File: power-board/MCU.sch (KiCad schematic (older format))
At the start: 29 parts, among them CON1 AVR-ISP-6, IC1 ATMEGA328P-A, SW1 BOOT, SW2 RESET, Y1 20MHz

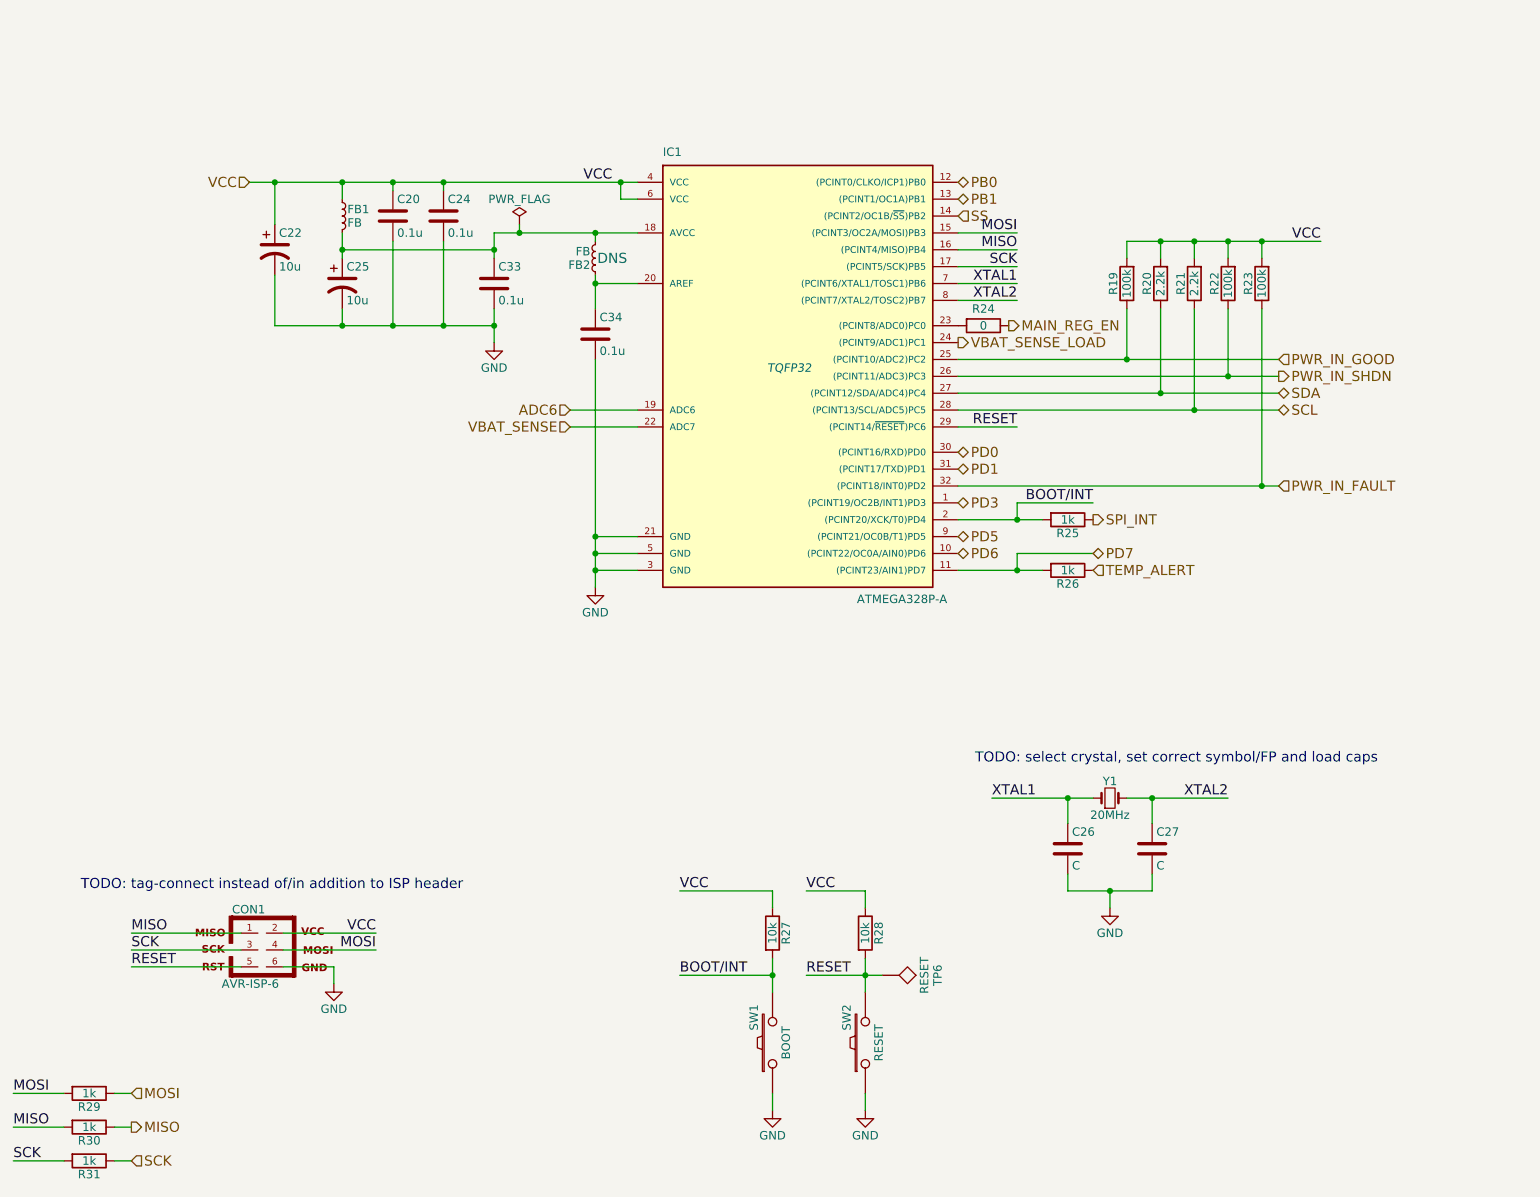
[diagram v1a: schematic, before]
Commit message: switched to XMEGA A4U
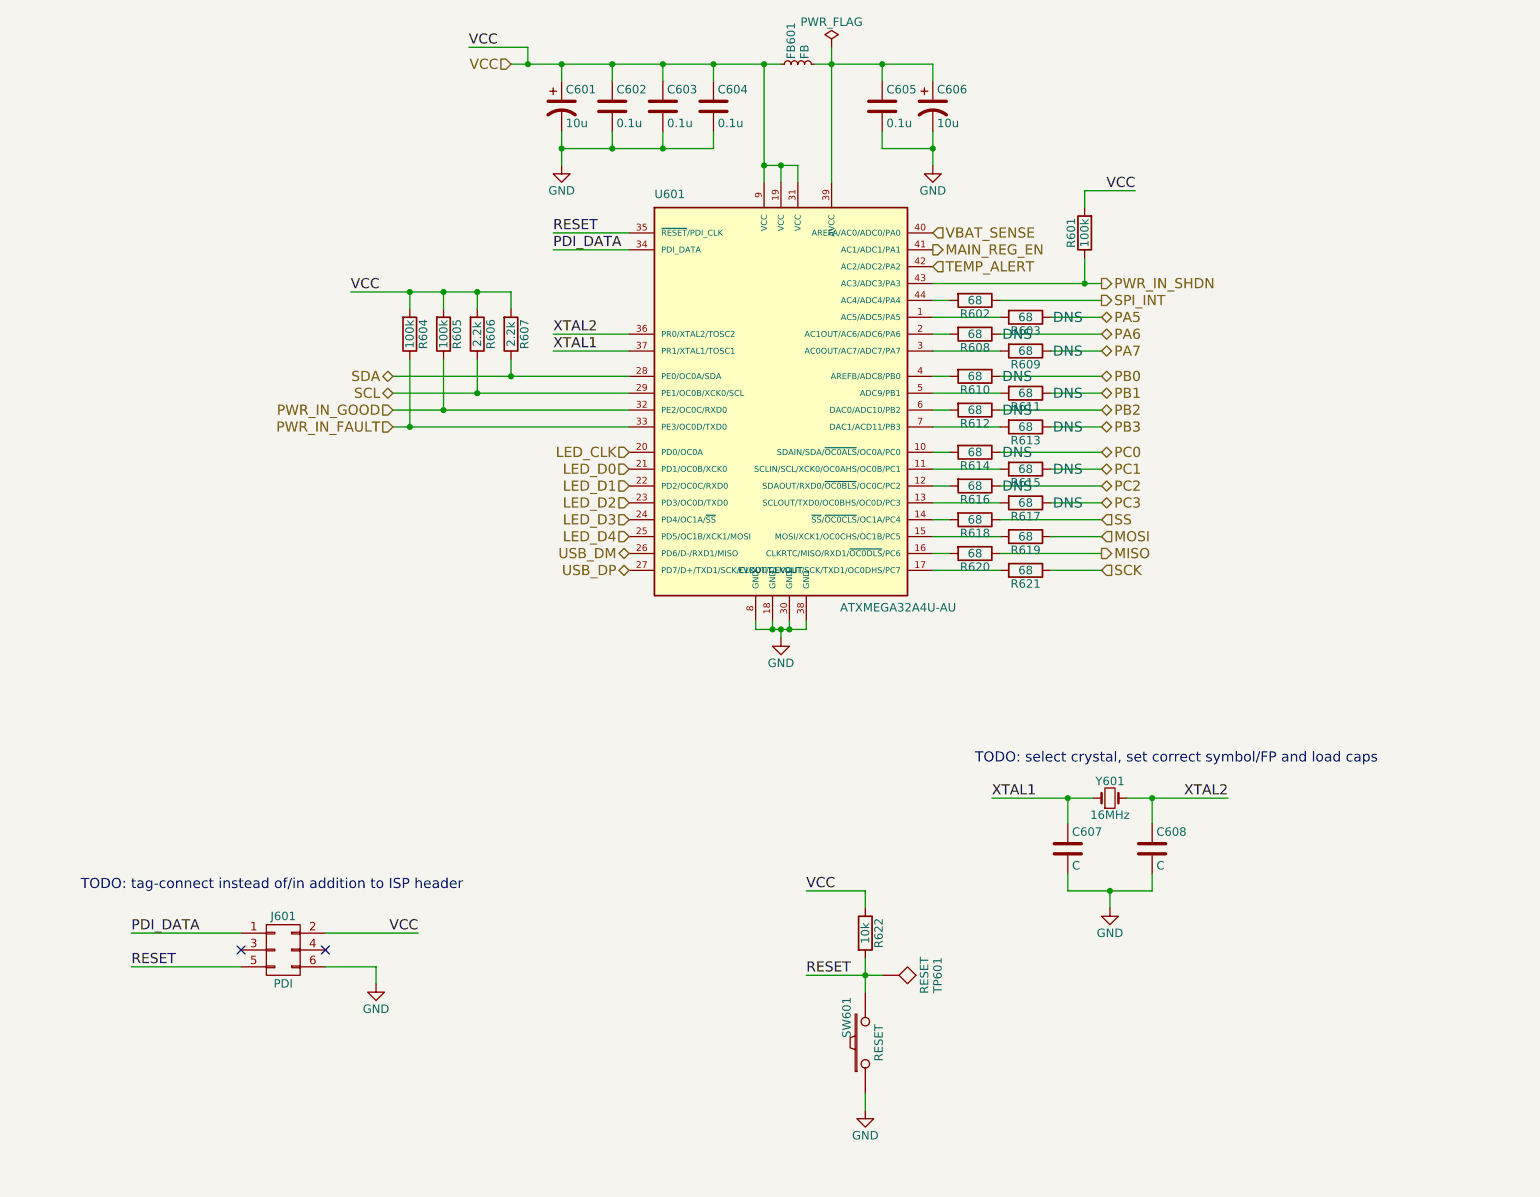
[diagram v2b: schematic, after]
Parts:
- removed C24, C33, C34: 0.1u, symbol C
- removed CON1: AVR-ISP-6, AVR-ISP-6, symbol AVR-ISP-6
- removed FB2: FB, symbol L_Small
- removed IC1: ATMEGA328P-A, TQFP32, symbol ATMEGA328P-A
- removed R24: 0, symbol R
- removed R25, R26, R29, R30, R31: 1k, symbol R
- removed R27: 10k, symbol R
- removed SW1: BOOT, symbol SW_PUSH
- added C603, C604, C605: 0.1u, symbol C
- added J601: PDI, symbol CONN_02X03
- added R602, R603, R608, R609, R610, R611, R612, R613, R614, R615, R616, R617, R618, R619, R620, R621: 68, symbol R
- added U601: ATXMEGA32A4U-AU, TQFP44, symbol ATXMEGA32A4U-AU
- Y601: renamed from Y1; value 20MHz -> 16MHz
- renumbered C22 to C601, C20 to C602, C25 to C606, C26 to C607, C27 to C608, FB1 to FB601, R23 to R601, R22 to R604, R19 to R605, R21 to R606, R20 to R607, R28 to R622, SW2 to SW601, TP6 to TP601
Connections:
- net GND: now also C603.2, C604.2, C605.2, J601.6 (P6), U601.18 (GND), U601.30 (GND), U601.38 (GND), U601.8 (GND)
- net MAIN_REG_EN: now also U601.41 (AC1/ADC1/PA1)
- net MISO: now also R620.1
- net MOSI: now also R619.1
- net PB0: now also R610.1
- net PB1: now also R611.1
- net PWR_IN_FAULT: now also R604.1, U601.33 (PE3/OC0D/TXD0); no longer R601.1
- net PWR_IN_GOOD: now also U601.32 (PE2/OC0C/RXD0)
- net PWR_IN_SHDN: now also R601.1, U601.43 (AC3/ADC3/PA3); no longer R604.1
- net RESET: now also J601.5 (P5), U601.35 (~RESET~/PDI_CLK)
- net SCK: now also R621.1
- net SCL: now also U601.29 (PE1/OC0B/XCK0/SCL)
- net SDA: now also U601.28 (PE0/OC0A/SDA)
- net SPI_INT: now also R602.1
- net SS: now also R618.1
- net TEMP_ALERT: now also U601.42 (AC2/ADC2/PA2)
- net VBAT_SENSE: now also U601.40 (AREFA/AC0/ADC0/PA0)
- net VCC: now also C603.1, C604.1, J601.2 (P2), U601.19 (VCC), U601.31 (VCC), U601.9 (VCC)
- net XTAL1: now also U601.37 (PR1/XTAL1/TOSC1)
- net XTAL2: now also U601.36 (PR0/XTAL2/TOSC2)
- net at C606.1, FB601.2: now also C605.1, U601.39 (AVCC)
- new net: R603.2, U601.1 (AC5/ADC5/PA5)
- new net: R614.2, U601.10 (SDAIN/SDA/~OC0ALS~/OC0A/PC0)
- new net: R615.2, U601.11 (SCLIN/SCL/XCK0/OC0AHS/OC0B/PC1)
- new net: R616.2, U601.12 (SDAOUT/RXD0/~OC0BLS~/OC0C/PC2)
- new net: R617.2, U601.13 (SCLOUT/TXD0/OC0BHS/OC0D/PC3)
- new net: R618.2, U601.14 (~SS~/~OC0CLS~/OC1A/PC4)
- new net: R619.2, U601.15 (MOSI/XCK1/OC0CHS/OC1B/PC5)
- new net: R620.2, U601.16 (CLKRTC/MISO/RXD1/~OC0DLS~/PC6)
- new net: R621.2, U601.17 (EVOUT/CLKOUT/SCK/TXD1/OC0DHS/PC7)
- new net: R608.2, U601.2 (AC1OUT/AC6/ADC6/PA6)
- new net: R609.2, U601.3 (AC0OUT/AC7/ADC7/PA7)
- new net: R610.2, U601.4 (AREFB/ADC8/PB0)
- new net: R602.2, U601.44 (AC4/ADC4/PA4)
- new net: R611.2, U601.5 (ADC9/PB1)
- new net: R612.2, U601.6 (DAC0/ADC10/PB2)
- new net: R613.2, U601.7 (DAC1/ACD11/PB3)
- new net LED_CLK: U601.20 (PD0/OC0A)
- new net LED_D0: U601.21 (PD1/OC0B/XCK0)
- new net LED_D1: U601.22 (PD2/OC0C/RXD0)
- new net LED_D2: U601.23 (PD3/OC0D/TXD0)
- new net LED_D3: U601.24 (PD4/OC1A/~SS~)
- new net LED_D4: U601.25 (PD5/OC1B/XCK1/MOSI)
- new net PA5: R603.1
- new net PA6: R608.1
- new net PA7: R609.1
- new net PB2: R612.1
- new net PB3: R613.1
- new net PC0: R614.1
- new net PC1: R615.1
- new net PC2: R616.1
- new net PC3: R617.1
- new net PDI_DATA: J601.1 (P1), U601.34 (PDI_DATA)
- new net USB_DM: U601.26 (PD6/D-/RXD1/MISO)
- new net USB_DP: U601.27 (PD7/D+/TXD1/SCK/CLKOUT/EVOUT)
- no-connect marks 0 -> 2
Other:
- moved on the sheet: C601, C602, C606, FB601, R601, R604, R605, R606, R607

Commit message: routed board
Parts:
- C601, C606: footprint (none) -> Capacitors_SMD:C_0805
- C602, C603, C604, C605: footprint (none) -> Capacitors_SMD:C_0603
- C607, C608: value C -> 26p; footprint (none) -> Capacitors_SMD:C_0805; MFG (none) -> Johanson Dielectrics Inc.; MPN (none) -> 500R15N270KV4T
- FB601: footprint (none) -> Resistors_SMD:R_0805; MFG (none) -> TDK; MPN (none) -> MPZ2012S102AT000
- J601: footprint (none) -> Connectors:Tag-Connect_TC2030-IDC-NL
- R601: value 100k -> 68; footprint (none) -> Resistors_SMD:R_0603; MFG Vishay / Draloric -> Yageo; MPN RCA0603100KJNEC -> RC0603JR-0768RL; Note (none) -> DNS
- R602, R603, R608, R609, R610, R611, R612, R613, R614, R615, R618, R619, R620, R621: footprint (none) -> Resistors_SMD:R_0603; MFG (none) -> Yageo; MPN (none) -> RC0603JR-0768RL
- R604, R605: footprint (none) -> Resistors_SMD:R_0603; MFG Vishay / Draloric -> Yageo; MPN RCA0603100KJNEC -> RC0603JR-07100KL
- R606, R607: footprint (none) -> Resistors_SMD:R_0603; MFG (none) -> Yageo; MPN (none) -> RC0603JR-072K2L
- R616, R617: footprint (none) -> Resistors_SMD:R_0603; MFG (none) -> Yageo; MPN (none) -> RC0603JR-0768RL; Note DNS -> (none)
- R622: footprint (none) -> Resistors_SMD:R_0603
- SW601: footprint (none) -> Buttons_Switches_SMD:SW_SPST_EVPBF; MFG TE Connectivity -> Panasonic Electronic Components; MPN FSM2JSMAATR -> EVP-BFAC1A000
- TP601: footprint (none) -> Connectors:PINTST
- U601: footprint TQFP44 -> Housings_QFP:TQFP-44_10x10mm_Pitch0.8mm; MFG (none) -> Microchip Technology; MPN (none) -> ATXMEGA32A4U-AU
- Y601: footprint (none) -> Crystals:Crystal_SMD_Abracon_ABM3-2pin_5.0x3.2mm_HandSoldering; MFG (none) -> Abracon; MPN (none) -> ABM3-16.000MHZ-B2-T; Note (none) -> DNS
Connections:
- net PWR_IN_SHDN: no longer U601.43 (AC3/ADC3/PA3)
- net VCC: no longer R601.2
- net PC2 renamed MASTER_SYNC
- net PC3 renamed SLAVE_SYNC
- new net: R601.2, U601.43 (AC3/ADC3/PA3)
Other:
- note removed: "TODO: select crystal, set correct symbol/FP and load caps"
- moved on the sheet: C607
